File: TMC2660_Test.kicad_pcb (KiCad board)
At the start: 2 copper layers, 77.7 x 49.9 mm, 71 parts, among them M101 LOGO_OSHW, P101 CONN_4, P102 CONN_4, P103 CONN_2, P104 CONN_13X2, P105 CONN_4, P106 CONN_4, P107 CONN_1, P108 CONN_1, P109 CONN_1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

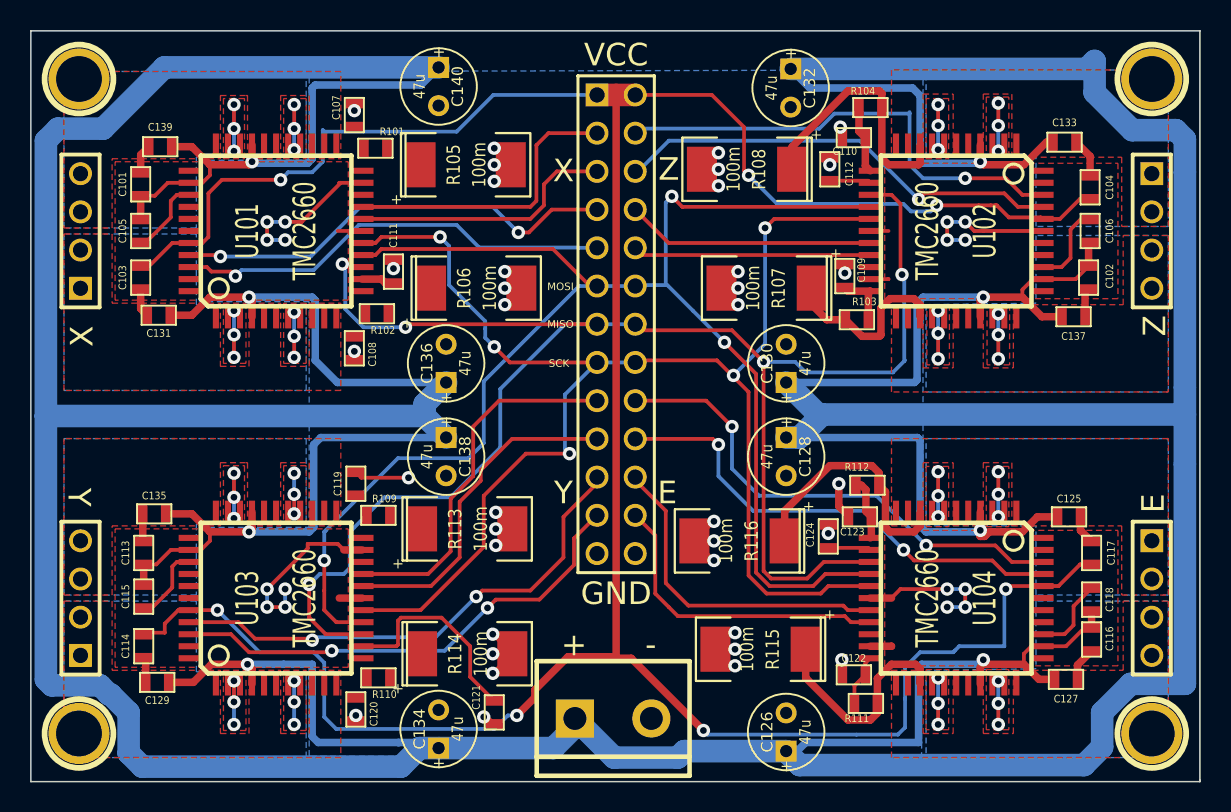
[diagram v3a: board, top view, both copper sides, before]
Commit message: Fix resistors, beef up current detection traces.
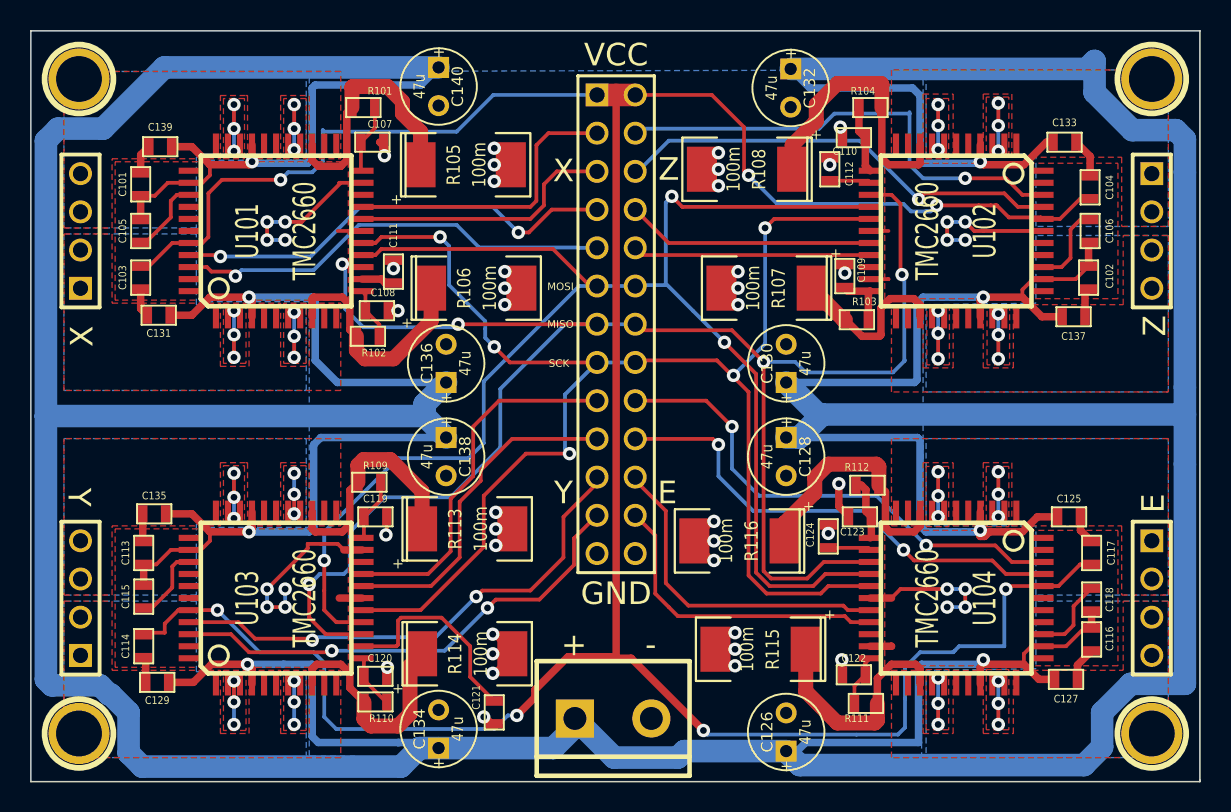
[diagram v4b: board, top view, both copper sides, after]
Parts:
- moved C108 2.92 mm to (158.3, 110.7), turned to 0 degrees
- moved R101 2.82 mm to (157.4, 97.2)
- moved C119 2.56 mm to (158.2, 124.4), turned to 0 degrees
- moved C120 2.56 mm to (158.2, 135.0), turned to 0 degrees
- moved R109 2.28 mm to (157.8, 122.1)
- moved C107 2.16 mm to (158.0, 99.5), turned to 0 degrees
- moved R102 1.62 mm to (157.7, 112.4)
- moved R110 1.61 mm to (158.2, 136.7)
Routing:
- net N-0000054: track 0.00 -> 17.1 mm
- net N-0000024: track 0.00 -> 15.8 mm
- net N-0000052: track 0.00 -> 15.6 mm
- net N-0000025: track 0.00 -> 15.2 mm
- net N-0000053: track 0.00 -> 4.61 mm
- net N-0000023: track 0.00 -> 4.22 mm
- net N-0000021: track 0.00 -> 3.62 mm
- net N-0000055: track 0.00 -> 3.47 mm
- net N-0000086: track 17.3 -> 18.8 mm
- net GND: track 112.1 -> 110.8 mm
- net N-0000047: track 14.7 -> 15.7 mm
- net N-0000085: track 12.2 -> 11.6 mm
